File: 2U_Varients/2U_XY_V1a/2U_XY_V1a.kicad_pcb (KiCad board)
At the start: 4 copper layers, 83 x 212.6 mm, 28 parts, among them CN1 DF11-2DSA-4DP, J2 Conn_01x01, J3 Conn_01x01, J4 Conn_01x01, J5 Conn_01x01, U2 TMP112xxDRL, U3 DRV2605LDGS, U4 TCA4311ADGKR, U5 5040500691, U7 VEML6031X00

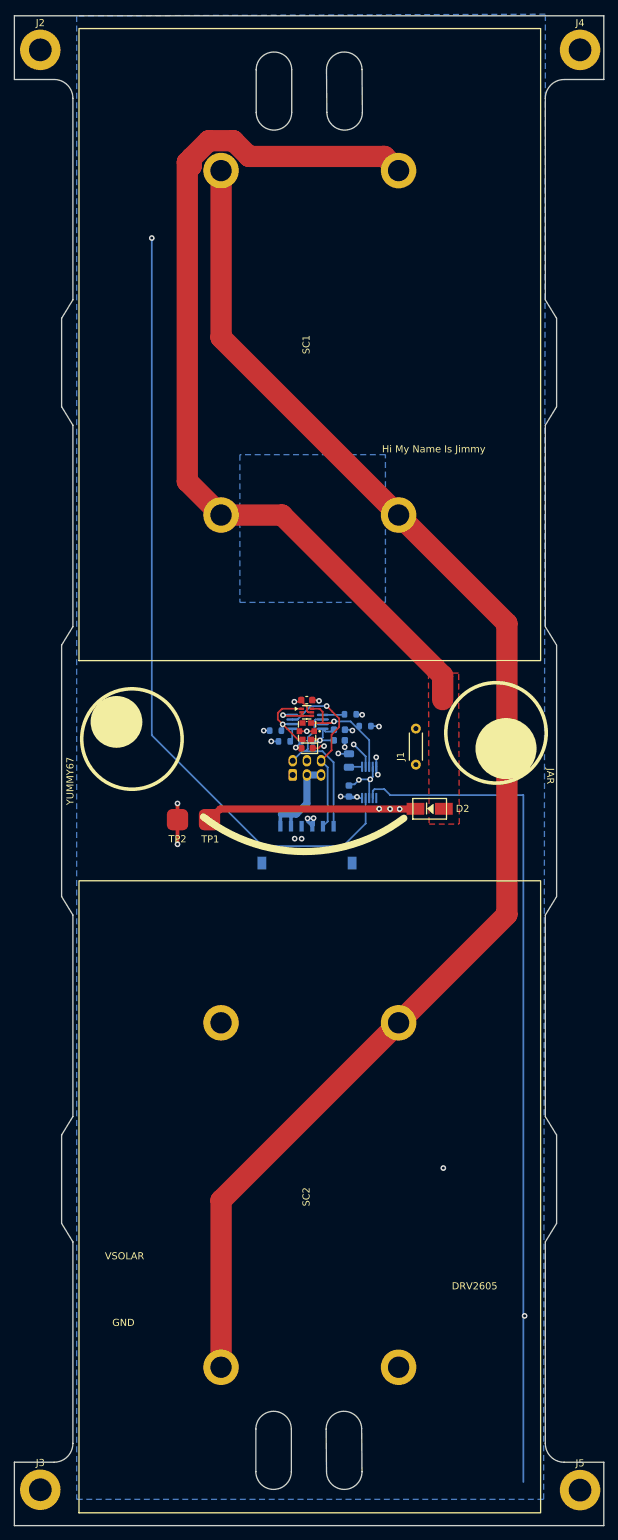
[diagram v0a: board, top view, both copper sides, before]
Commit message: Fastener Slots
Updated fastener slots so it fits with the structure
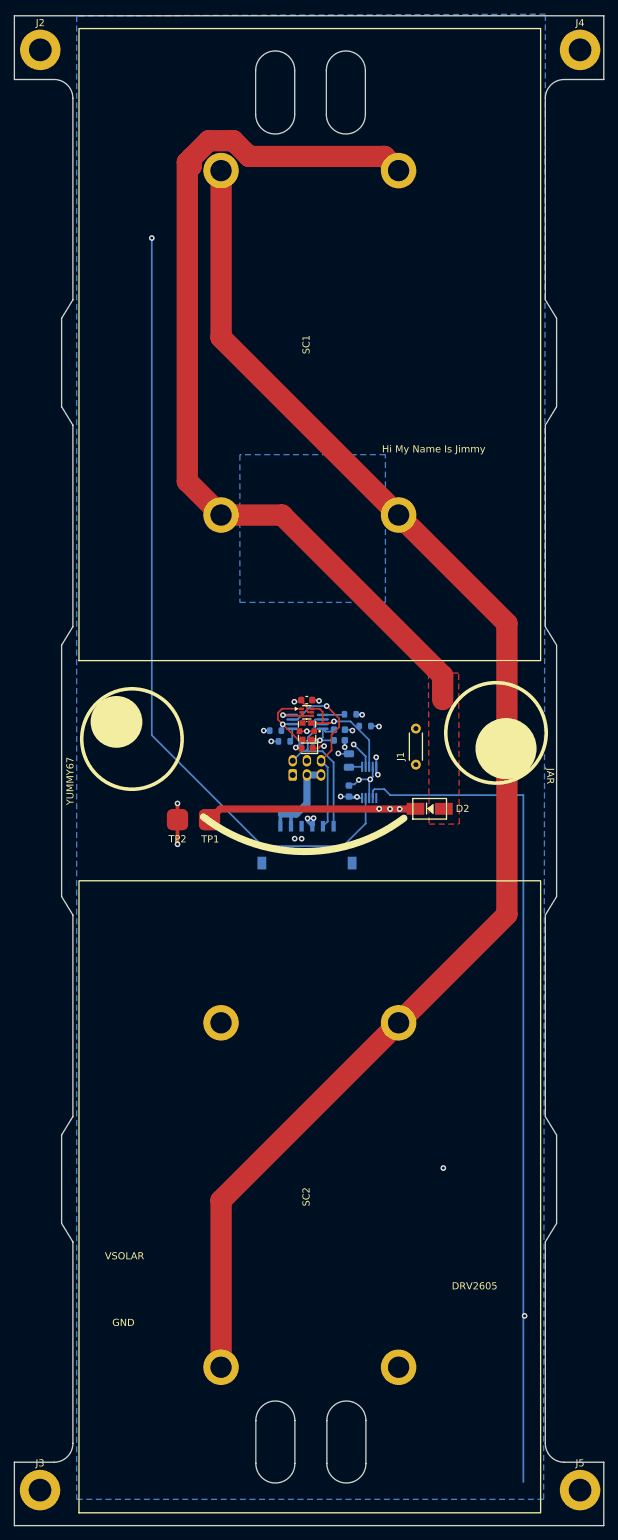
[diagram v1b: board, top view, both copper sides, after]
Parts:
- moved J3 0.06 mm to (171.8, 243.8)
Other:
- outline, holes or cut-outs redrawn

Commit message: Updated Production Files
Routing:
- net VSOLAR: track 43.4 -> 53.0 mm
- net /SOL_OUT: track 129.4 -> 131.0 mm
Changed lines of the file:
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@@
 			(psa4output no)
 			(plot_black_and_white yes)
+			(plotinvisibletext no)
 			(sketchpadsonfab no)
 			(plotpadnumbers no)
@@
 		(sheetname "/")
 		(sheetfile "2U_XY_V1a.kicad_sch")
-		(attr through_hole)
+		(attr through_hole exclude_from_pos_files exclude_from_bom)
 		(fp_line
 			(start 0.62 -0.92)
@@
 	)
 	(segment
+		(start 209.340001 147.832775)
+		(end 209.4 147.892774)
+		(width 1)
+		(layer "F.Cu")
+		(net 3)
+	)
+	(segment
+		(start 211.3 147.892774)
+		(end 209.4 147.892774)
+		(width 1)
+		(layer "F.Cu")
+		(net 3)
+	)
+	(segment
+		(start 209.340001 143.099999)
+		(end 209.340001 147.832775)
+		(width 1)
+		(layer "F.Cu")
+		(net 3)
+	)
+	(segment
+		(start 211.34 143.099999)
+		(end 211.34 147.852774)
+		(width 1)
+		(layer "F.Cu")
+		(net 3)
+	)
+	(segment
 		(start 197.120598 147.892774)
 		(end 195.620598 149.392774)
@@
 	(segment
 		(start 224.620596 147.892774)
+		(end 211.3 147.892774)
+		(width 1)
+		(layer "F.Cu")
+		(net 3)
+	)
+	(segment
+		(start 209.4 147.892774)
 		(end 197.120598 147.892774)
 		(width 1)
@@
 		(net 3)
 	)
+	(segment
+		(start 211.34 147.852774)
+		(end 211.3 147.892774)
+		(width 1)
+		(layer "F.Cu")
+		(net 3)
+	)
 	(via
 		(at 221.050596 147.882774)
@@
 	)
 	(segment
-		(start 198.990112 53.799)
-		(end 195.509888 53.799)
-		(width 3)
-		(layer "F.Cu")
-		(net 22)
-	)
-	(segment
-		(start 201.191112 56)
-		(end 198.990112 53.799)
+		(start 195.3 52.8)
+		(end 200.8 52.8)
 		(width 3)
 		(layer "F.Cu")
@@
 	)
 	(segment
-		(start 192.5 101.75)
-		(end 197.25 106.5)
-		(width 3)
-		(layer "F.Cu")
-		(net 22)
-	)
-	(segment
-		(start 192.5 56.808888)
-		(end 192.5 101.75)
+		(start 197.25 106.5)
+		(end 191.2 100.45)
 		(width 3)
 		(layer "F.Cu")
@@
 	)
 	(segment
-		(start 195.509888 53.799)
-		(end 193.049 56.259888)
+		(start 200.8 52.8)
+		(end 204 56)
 		(width 3)
 		(layer "F.Cu")
@@
 	)
 	(segment
-		(start 220.25 56)
-		(end 201.191112 56)
+		(start 204 56)
+		(end 220.25 56)
 		(width 3)
 		(layer "F.Cu")
@@
 	)
 	(segment
-		(start 193.049 56.259888)
-		(end 193.049 57.357888)
+		(start 228.455 129.13)
+		(end 228.455 132.5)
 		(width 3)
 		(layer "F.Cu")
@@
 	)
 	(segment
-		(start 228.455 129.13)
-		(end 228.455 132.5)
+		(start 205.825 106.5)
+		(end 228.455 129.13)
 		(width 3)
 		(layer "F.Cu")
@@
 	)
 	(segment
-		(start 205.825 106.5)
-		(end 228.455 129.13)
+		(start 197.25 106.5)
+		(end 205.825 106.5)
 		(width 3)
 		(layer "F.Cu")
@@
 	)
 	(segment
-		(start 193.049 57.357888)
-		(end 192.5 56.808888)
+		(start 191.2 56.9)
+		(end 195.3 52.8)
 		(width 3)
 		(layer "F.Cu")
@@
 	)
 	(segment
-		(start 197.25 106.5)
-		(end 205.825 106.5)
+		(start 220.25 56)
+		(end 222.25 58)
 		(width 3)
 		(layer "F.Cu")
@@
 	)
 	(segment
-		(start 222.25 58)
-		(end 220.25 56)
+		(start 191.2 100.45)
+		(end 191.2 56.9)
 		(width 3)
 		(layer "F.Cu")
